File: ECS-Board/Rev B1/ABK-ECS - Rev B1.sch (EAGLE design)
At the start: 298 parts, among them J1 USB-B-S-RA, J10 FTSH-105-01-L-DV-NOPASTE, J11 22-05-7028-02, J12 RB1-125BAG1A, J13 22-05-7068-06, J14 22-05-7048-04, J15 22-05-7048-04, J16 22-05-7048-04, J2 MSTBA2, J3 22-05-7068-06, J5 22-05-7068-06, J6 22-05-7068-06, J7 22-05-7068-06, J8 22-05-7028-02, J9 FTSH-103-01-L-DV-NOPASTE, SW1 B3FS-1015, SW2 B3FS-1015, T1 MMBT2907ALT3, T10 MMBT2222AL, T11 IRLML5103TRPBF, T12 MMBT2222AL, T13 IRLML5103TRPBF, T14 IRLML5103TRPBF, T15 IRLML5103TRPBF, T16 IRLML5103TRPBF, T17 MMBT2222AL, T18 MMBT2222AL, T19 MMBT2222AL, T2 EXMACHINA-LOGO-NAME, T20 MMBT2222AL, T3 IRLML5103TRPBF, T4 IRLML5103TRPBF, T5 IRLML5103TRPBF, T6 IRLML5103TRPBF, T7 MMBT2222AL, T8 MMBT2222AL, T9 MMBT2222AL, U1 AT24C512C-SSHM-B, U10 SN74LVC2G17DBVR, U2 LPC1768FBD100, U3 LT3686HDDPBF, U4 LT3686HDDPBF, U5 CD4050BD, U6 CD4050BD, U7 DP83848JSQ/NOPB, U9 SN74LVC2G17DBVR, X1 FC-135, X2 ASE-12, X3 3000, X4 ASE_50

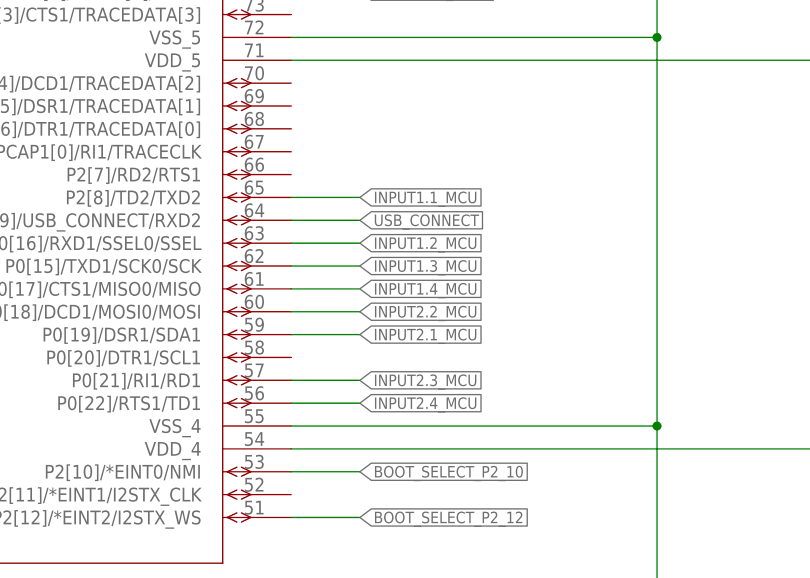
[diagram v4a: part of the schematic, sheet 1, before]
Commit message: Re-Map MCU output signal
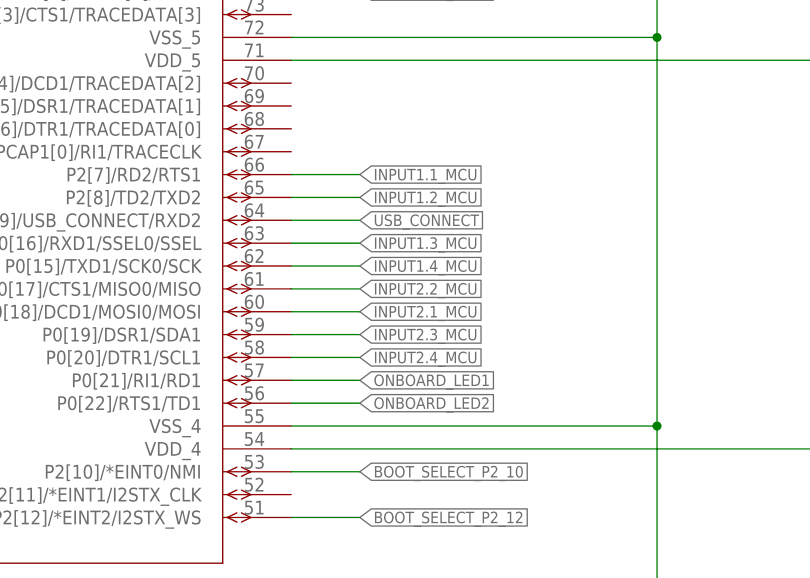
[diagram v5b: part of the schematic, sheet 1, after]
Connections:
- net INPUT1.1_MCU: now also U2.P2[7]/RD2/RTS1; no longer U2.P2[8]/TD2/TXD2
- net INPUT1.2_MCU: now also U2.P2[8]/TD2/TXD2; no longer U2.P0[16]/RXD1/SSEL0/SSEL
- net INPUT1.3_MCU: now also U2.P0[16]/RXD1/SSEL0/SSEL; no longer U2.P0[15]/TXD1/SCK0/SCK
- net INPUT1.4_MCU: now also U2.P0[15]/TXD1/SCK0/SCK; no longer U2.P0[17]/CTS1/MISO0/MISO
- net INPUT2.1_MCU: now also U2.P0[18]/DCD1/MOSI0/MOSI; no longer U2.P0[19]/DSR1/SDA1
- net INPUT2.2_MCU: now also U2.P0[17]/CTS1/MISO0/MISO; no longer U2.P0[18]/DCD1/MOSI0/MOSI
- net INPUT2.3_MCU: now also U2.P0[19]/DSR1/SDA1; no longer U2.P0[21]/RI1/RD1
- net INPUT2.4_MCU: now also U2.P0[20]/DTR1/SCL1; no longer U2.P0[22]/RTS1/TD1
- net ONBOARD_LED1: now also U2.P0[21]/RI1/RD1
- net ONBOARD_LED2: now also U2.P0[22]/RTS1/TD1
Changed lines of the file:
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@@
 <label x="325.12" y="170.18" size="1.27" layer="95" font="vector" xref="yes"/>
+</segment>
+<segment>
+<wire x1="325.12" y1="124.46" x2="317.5" y2="124.46" width="0.1524" layer="91"/>
+<label x="325.12" y="124.46" size="1.27" layer="95" font="vector" xref="yes"/>
+<pinref part="U2" gate="A" pin="P0[21]/RI1/RD1"/>
 </segment>
 </net>
@@
 <label x="325.12" y="167.64" size="1.27" layer="95" font="vector" xref="yes"/>
 </segment>
+<segment>
+<wire x1="325.12" y1="121.92" x2="317.5" y2="121.92" width="0.1524" layer="91"/>
+<label x="325.12" y="121.92" size="1.27" layer="95" font="vector" xref="yes"/>
+<pinref part="U2" gate="A" pin="P0[22]/RTS1/TD1"/>
+</segment>
 </net>
 <net name="!JTAG_TRST" class="0">
@@
 <net name="INPUT2.3_MCU" class="0">
 <segment>
-<pinref part="U2" gate="A" pin="P0[21]/RI1/RD1"/>
-<wire x1="317.5" y1="124.46" x2="325.12" y2="124.46" width="0.1524" layer="91"/>
-<label x="325.12" y="124.46" size="1.27" layer="95" font="vector" xref="yes"/>
-</segment>
-</net>
-<net name="INPUT2.1_MCU" class="0">
-<segment>
-<pinref part="U2" gate="A" pin="P0[19]/DSR1/SDA1"/>
 <wire x1="317.5" y1="129.54" x2="325.12" y2="129.54" width="0.1524" layer="91"/>
 <label x="325.12" y="129.54" size="1.27" layer="95" font="vector" xref="yes"/>
-</segment>
-</net>
-<net name="INPUT2.2_MCU" class="0">
-<segment>
-<pinref part="U2" gate="A" pin="P0[18]/DCD1/MOSI0/MOSI"/>
+<pinref part="U2" gate="A" pin="P0[19]/DSR1/SDA1"/>
+</segment>
+</net>
+<net name="INPUT2.1_MCU" class="0">
+<segment>
 <wire x1="317.5" y1="132.08" x2="325.12" y2="132.08" width="0.1524" layer="91"/>
 <label x="325.12" y="132.08" size="1.27" layer="95" font="vector" xref="yes"/>
+<pinref part="U2" gate="A" pin="P0[18]/DCD1/MOSI0/MOSI"/>
+</segment>
+</net>
+<net name="INPUT2.2_MCU" class="0">
+<segment>
+<wire x1="317.5" y1="134.62" x2="325.12" y2="134.62" width="0.1524" layer="91"/>
+<label x="325.12" y="134.62" size="1.27" layer="95" font="vector" xref="yes"/>
+<pinref part="U2" gate="A" pin="P0[17]/CTS1/MISO0/MISO"/>
 </segment>
 </net>
 <net name="INPUT2.4_MCU" class="0">
 <segment>
-<pinref part="U2" gate="A" pin="P0[22]/RTS1/TD1"/>
-<wire x1="317.5" y1="121.92" x2="325.12" y2="121.92" width="0.1524" layer="91"/>
-<label x="325.12" y="121.92" size="1.27" layer="95" font="vector" xref="yes"/>
+<wire x1="317.5" y1="127" x2="325.12" y2="127" width="0.1524" layer="91"/>
+<label x="325.12" y="127" size="1.27" layer="95" font="vector" xref="yes"/>
+<pinref part="U2" gate="A" pin="P0[20]/DTR1/SCL1"/>
 </segment>
 </net>
@@
 <net name="INPUT1.4_MCU" class="0">
 <segment>
-<wire x1="325.12" y1="134.62" x2="317.5" y2="134.62" width="0.1524" layer="91"/>
-<label x="325.12" y="134.62" size="1.27" layer="95" font="vector" xref="yes"/>
-<pinref part="U2" gate="A" pin="P0[17]/CTS1/MISO0/MISO"/>
+<wire x1="325.12" y1="137.16" x2="317.5" y2="137.16" width="0.1524" layer="91"/>
+<label x="325.12" y="137.16" size="1.27" layer="95" font="vector" xref="yes"/>
+<pinref part="U2" gate="A" pin="P0[15]/TXD1/SCK0/SCK"/>
 </segment>
 </net>
 <net name="INPUT1.2_MCU" class="0">
 <segment>
-<pinref part="U2" gate="A" pin="P0[16]/RXD1/SSEL0/SSEL"/>
+<wire x1="317.5" y1="144.78" x2="325.12" y2="144.78" width="0.1524" layer="91"/>
+<label x="325.12" y="144.78" size="1.27" layer="95" font="vector" xref="yes"/>
+<pinref part="U2" gate="A" pin="P2[8]/TD2/TXD2"/>
+</segment>
+</net>
+<net name="INPUT1.3_MCU" class="0">
+<segment>
 <wire x1="317.5" y1="139.7" x2="325.12" y2="139.7" width="0.1524" layer="91"/>
 <label x="325.12" y="139.7" size="1.27" layer="95" font="vector" xref="yes"/>
-</segment>
-</net>
-<net name="INPUT1.3_MCU" class="0">
-<segment>
-<wire x1="317.5" y1="137.16" x2="325.12" y2="137.16" width="0.1524" layer="91"/>
-<label x="325.12" y="137.16" size="1.27" layer="95" font="vector" xref="yes"/>
-<pinref part="U2" gate="A" pin="P0[15]/TXD1/SCK0/SCK"/>
+<pinref part="U2" gate="A" pin="P0[16]/RXD1/SSEL0/SSEL"/>
 </segment>
 </net>
@@
 <net name="INPUT1.1_MCU" class="0">
 <segment>
-<wire x1="317.5" y1="144.78" x2="325.12" y2="144.78" width="0.1524" layer="91"/>
-<pinref part="U2" gate="A" pin="P2[8]/TD2/TXD2"/>
-<label x="325.12" y="144.78" size="1.27" layer="95" font="vector" xref="yes"/>
-</segment>
-</net>
+<wire x1="317.5" y1="147.32" x2="325.12" y2="147.32" width="0.1524" layer="91"/>
+<label x="325.12" y="147.32" size="1.27" layer="95" font="vector" xref="yes"/>
+<pinref part="U2" gate="A" pin="P2[7]/RD2/RTS1"/>
+</segment>
+</net>

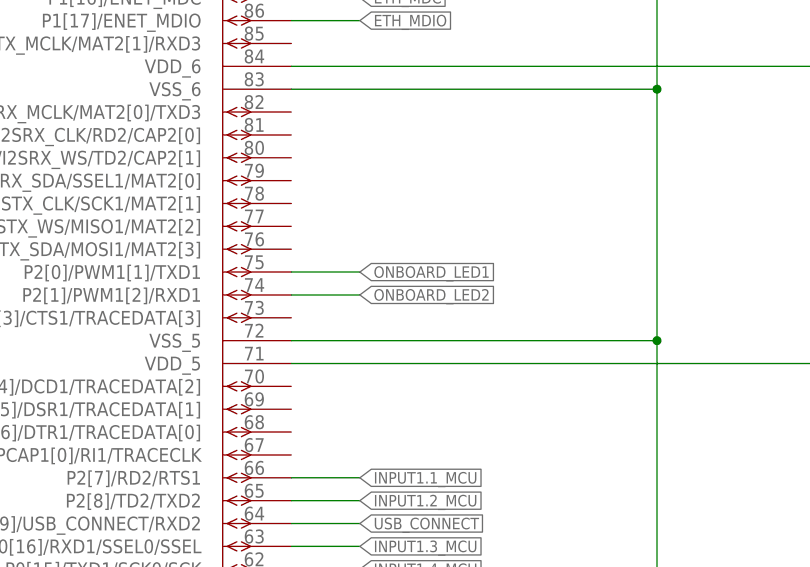
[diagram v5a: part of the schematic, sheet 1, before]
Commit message: Route Reset and all airwire
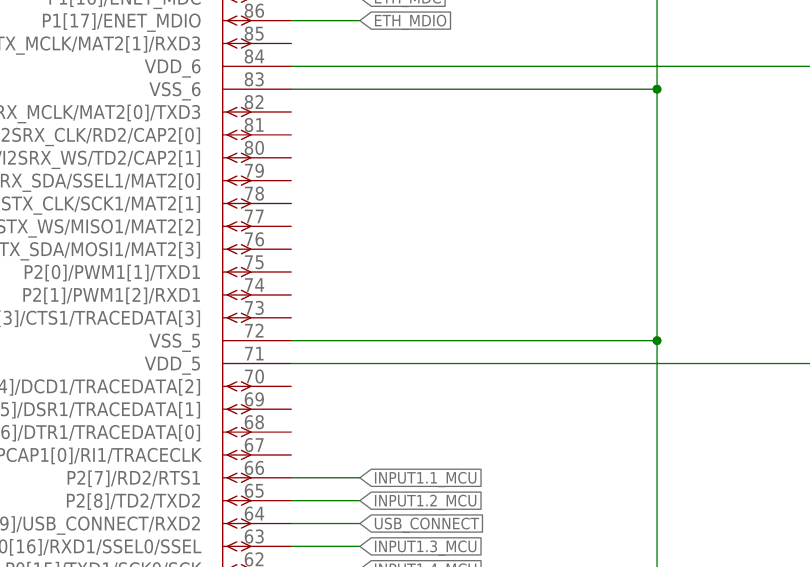
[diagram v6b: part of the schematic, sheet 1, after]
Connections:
- net ONBOARD_LED1: no longer U2.P2[0]/PWM1[1]/TXD1
- net ONBOARD_LED2: no longer U2.P2[1]/PWM1[2]/RXD1
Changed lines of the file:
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@@
-</segment>
-<segment>
-<wire x1="325.12" y1="170.18" x2="317.5" y2="170.18" width="0.1524" layer="91"/>
-<pinref part="U2" gate="A" pin="P2[0]/PWM1[1]/TXD1"/>
-<label x="325.12" y="170.18" size="1.27" layer="95" font="vector" xref="yes"/>
 </segment>
 <segment>
@@
 </segment>
 <segment>
-<wire x1="325.12" y1="167.64" x2="317.5" y2="167.64" width="0.1524" layer="91"/>
-<pinref part="U2" gate="A" pin="P2[1]/PWM1[2]/RXD1"/>
-<label x="325.12" y="167.64" size="1.27" layer="95" font="vector" xref="yes"/>
-</segment>
-<segment>

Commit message: Improte routing and add Silkscreen
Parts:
- removed C36: 0.1uF, rcl:C-EUC0603
- removed D13: 1N4148WS, diode:1N4148WS
- removed J16: 22-05-7048-04, con-molex:22-05-7048-04
- removed R153, R154: 1K, rcl:R-EU_R0603
- removed U10: SN74LVC2G17DBVR, ti:SN74LVC2G17DBVR
- added C20: 0.1uF, rcl:C-EUC0603
- added D4: 1N4148WS, diode:1N4148WS
- added J4: 22-05-7068-06, con-molex:22-05-7068-06
- added R40: 4K7, rcl:R-EU_R0603
- added R41: 1K, rcl:R-EU_R0603
- added U8: SN74LVC2G17DBVR, ti:SN74LVC2G17DBVR
- C22: value 0.1uF -> 4.7uF; device rcl:C-EUC0603 -> rcl:CPOL-EUCT3216; MPN MC0603B104K160CT -> F931A475MAA; OC_NEWARK 06R4923 -> 58R3271
- C23: value 4.7uF -> 100nF; device rcl:CPOL-EUCT3216 -> rcl:C-EUC0603; MPN F931A475MAA -> MC0603B104K250CT; OC_NEWARK 58R3271 -> 06R4925
- C25, C29: value 100nF -> 10uF; device rcl:C-EUC0603 -> rcl:CPOL-EUCT3216; MPN MC0603B104K250CT -> F931A106MAA; OC_NEWARK 06R4925 -> 58R3260
- C26, C30: value 10uF -> 100nF; device rcl:CPOL-EUCT3216 -> rcl:C-EUC0603; MPN F931A106MAA -> MC0603B104K250CT; OC_NEWARK 58R3260 -> 06R4925
- C34: value 100nF -> 0.1uF; MPN MC0603B104K250CT -> MC0603B104K160CT; OC_NEWARK 06R4925 -> 06R4923
- J10: value FTSH-105-01-L-DV-NOPASTE -> 22-05-7028-02; device con-samtec:FTSH-105-01-L-DV-NOPASTE -> con-molex:22-05-7028-02; MPN (none) -> 22-05-7028; OC_NEWARK (none) -> 25M1728
- J11: value 22-05-7028-02 -> RB1-125BAG1A; device con-molex:22-05-7028-02 -> con-wiznet:RB1-125BAG1A; MPN 22-05-7028 -> (none); OC_NEWARK 25M1728 -> unknown
- J12: value RB1-125BAG1A -> 22-05-7068-06; device con-wiznet:RB1-125BAG1A -> con-molex:22-05-7068-06; MF (none) -> MOLEX; MPN (none) -> 22-05-7058; OC_NEWARK unknown -> 55H9619
- J13: value 22-05-7068-06 -> 22-05-7048-04; device con-molex:22-05-7068-06 -> con-molex:22-05-7048-04; MF MOLEX -> (none); MPN 22-05-7058 -> (none); OC_NEWARK 55H9619 -> (none)
- J7: value 22-05-7068-06 -> 22-05-7028-02; device con-molex:22-05-7068-06 -> con-molex:22-05-7028-02; MPN (none) -> 22-05-7028; OC_NEWARK (none) -> 25M1728
- J8: value 22-05-7028-02 -> FTSH-103-01-L-DV-NOPASTE; device con-molex:22-05-7028-02 -> con-samtec:FTSH-103-01-L-DV-NOPASTE; MPN 22-05-7028 -> (none); OC_NEWARK 25M1728 -> (none)
- J9: value FTSH-103-01-L-DV-NOPASTE -> FTSH-105-01-L-DV-NOPASTE; device con-samtec:FTSH-103-01-L-DV-NOPASTE -> con-samtec:FTSH-105-01-L-DV-NOPASTE
- LED3: value Red -> Blue; MPN OVS-0608 -> OVS-0603; OC_NEWARK 15R2208 -> 15R2205
- LED4: value Blue -> Red; MPN OVS-0603 -> OVS-0608; OC_NEWARK 15R2205 -> 15R2208
- LED5: OC_FARNELL 1716771 -> (none)
- LED7: OC_FARNELL (none) -> 1716771
- MP1, MP2, MP3, MP4: value MOUNT-PAD3,0 -> MOUNT-PAD3.5; device holes:MOUNT-PAD3,0 -> holes:MOUNT-PAD3.5
- R10: value 10K -> 33; MPN RC0603FR-0710KL -> RC0603FR-0733RL; OC_NEWARK 68R0049 -> 68R0085
- R101, R70: value 10K -> 1K; MPN RC0603FR-0710KL -> RC0603FR-071KL; OC_NEWARK 68R0049 -> 68R0042
- R105, R74: value 1K -> 1K5; MPN RC0603FR-071KL -> RC0603FR-071K5L; OC_NEWARK 68R0042 -> 68R0045
- R109, R39, R78: value 1K5 -> 4K7; MPN RC0603FR-071K5L -> RC0603FR-074K7L; OC_NEWARK 68R0045 -> 68R0092
- R11: value 0R -> 33; MPN RC0603FR-070RL -> RC0603FR-0733RL; OC_NEWARK 50Y7761 -> 68R0085
- R113, R82: value 4K7 -> 100; MPN RC0603FR-074K7L -> RC0603FR-13100RL; OC_NEWARK 68R0092 -> 68R0131
- R117, R86: value 100 -> 330; MPN RC0603FR-13100RL -> RC0603FR-07330RL; OC_NEWARK 68R0131 -> 98K7391
- R12: value 0R -> 1K5; MPN RC0603FR-070RL -> RC0603FR-071K5L; OC_NEWARK 50Y7761 -> 68R0045
- R121: value 330 -> 0R; MPN RC0603FR-07330RL -> MCMR06X000 PTL; OC_NEWARK 98K7391 -> 86T3500
- R123: value 0R -> 220; MPN MCMR06X000 PTL -> MCMR06X2200FTL; OC_NEWARK 86T3500 -> 86T3577
- R125: value 220 -> 49.9; MPN MCMR06X2200FTL -> MCMR06X49R9FTL; OC_NEWARK 86T3577 -> 86T3659
- R129: value 49.9 -> 4K7; MPN MCMR06X49R9FTL -> MCMR06X4701FTL; OC_NEWARK 86T3659 -> 86T3649
- R130: value 4K7 -> 2K2; MPN MCMR06X4701FTL -> MCMR06X2201FTL; OC_NEWARK 86T3649 -> 86T3578
- R131: value 2K2 -> 1K; MPN MCMR06X2201FTL -> MCMR06X1001FTL; OC_NEWARK 86T3578 -> 86T3505
- R132: value 0R, DNI -> 1K; MPN RC0603FR-070RL -> MCMR06X1001FTL; OC_NEWARK 50Y7761 -> 86T3505
- R133, R138: value 4K7 -> 1K; MPN MCMR06X2701FTL -> MCMR06X1001FTL; OC_NEWARK 86T3598 -> 86T3505
- R134, R144: value 1K -> 4K7; MPN MCMR06X1001FTL -> MCMR06X2701FTL; OC_NEWARK 86T3505 -> 86T3598
- R14, R15: value 1K5 -> 0R; MPN RC0603FR-071K5L -> RC0603FR-070RL; OC_NEWARK 68R0045 -> 50Y7761
- R16: value 31K6 -> 10K; MPN MCMR06X3162FTL -> RC0603FR-0710KL; OC_FARNELL 2073391 -> (none); OC_NEWARK 86T3613 -> 68R0049
- R17: value 31K6 -> 1K5; MPN MCMR06X3162FTL -> RC0603FR-071K5L; OC_FARNELL 2073391 -> (none); OC_NEWARK 86T3613 -> 68R0045
- R18, R53: value 4K7 -> 1K5; MPN RC0603FR-074K7L -> RC0603FR-071K5L; OC_NEWARK 68R0092 -> 68R0045
- R19: value 4K7 -> 31K6; MPN RC0603FR-074K7L -> MCMR06X3162FTL; OC_FARNELL (none) -> 2073391; OC_NEWARK 68R0092 -> 86T3613
- R20: value 52K3 -> 31K6; MPN MC0063W0603152K3 -> MCMR06X3162FTL; OC_NEWARK 26M0962 -> 86T3613
- R21: value 10K -> 4K7; MPN RC0603FR-0710KL -> RC0603FR-074K7L; OC_FARNELL 2073391 -> (none); OC_NEWARK 68R0049 -> 68R0092
- R22: value 31K6 -> 4K7; MPN MCMR06X3162FTL -> RC0603FR-074K7L; OC_FARNELL 2073391 -> (none); OC_NEWARK 86T3613 -> 68R0092
- R23: value 10K -> 52K3; MPN RC0603FR-0710KL -> MC0063W0603152K3; OC_NEWARK 68R0049 -> 26M0962
- R24: value 1K5 -> 10K; MPN RC0603FR-071K5L -> RC0603FR-0710KL; OC_NEWARK 68R0045 -> 68R0049
- R25: value 1K5 -> 31K6; MPN RC0603FR-071K5L -> MCMR06X3162FTL; OC_NEWARK 68R0045 -> 86T3613
- R26: value 1K5 -> 10K; MPN RC0603FR-071K5L -> RC0603FR-0710KL; OC_FARNELL (none) -> 2073391; OC_NEWARK 68R0045 -> 68R0049
- R27, R28: value 1K -> 1K5; MPN RC0603FR-071KL -> RC0603FR-071K5L; OC_FARNELL (none) -> 2073391; OC_NEWARK 68R0042 -> 68R0045
- R35, R36: value 4K7 -> 1K; MPN RC0603FR-074K7L -> RC0603FR-071KL; OC_NEWARK 68R0092 -> 68R0042
- R49: value 1K -> 4K7; MPN RC0603FR-071KL -> RC0603FR-074K7L; OC_NEWARK 68R0042 -> 68R0092
- R5: value 39K -> 1K5; MPN (none) -> RC0603FR-071K5L; OC_NEWARK (none) -> 68R0045
- R6: value 24K -> 1K5; MPN (none) -> RC0603FR-071K5L; OC_NEWARK (none) -> 68R0045
- R62: value 1K5 -> 1K; device rcl:R-EU_R0603 -> rcl:R-EU_R1206; MPN RC0603FR-071K5L -> (none); OC_NEWARK 68R0045 -> (none)
- R66, R91, R97: value 1K -> 10K; device rcl:R-EU_R1206 -> rcl:R-EU_R0603; MPN (none) -> RC0603FR-0710KL; OC_NEWARK (none) -> 68R0049
- R7: value 33 -> 39K; MPN RC0603FR-0733RL -> (none); OC_NEWARK 68R0085 -> (none)
- R8: value 33 -> 24K; MPN RC0603FR-0733RL -> (none); OC_NEWARK 68R0085 -> (none)
- R9: value 1K5 -> 0R, DNI; MPN RC0603FR-071K5L -> RC0603FR-070RL; OC_NEWARK 68R0045 -> 50Y7761
- R90: value 330 -> 1K; device rcl:R-EU_R0603 -> rcl:R-EU_R1206; MPN RC0603FR-07330RL -> (none); OC_NEWARK 98K7391 -> (none)
- R92: value 10K -> 100; MPN RC0603FR-0710KL -> RC0603FR-13100RL; OC_NEWARK 68R0049 -> 68R0131
- R93: value 100 -> 1K; device rcl:R-EU_R0603 -> rcl:R-EU_R1206; MPN RC0603FR-13100RL -> (none); OC_NEWARK 68R0131 -> (none)
- SJ1, SJ2: value SOLDERJUMPERNC -> SJNC; device SparkFun-Passives:SOLDERJUMPERNC -> SparkFun-Passives:SJNC; OC_NEWARK unknown -> (none)
- SJ3, SJ4, SJ5: value SOLDERJUMPERNC -> SJNC; device SparkFun-Passives:SOLDERJUMPERNC -> SparkFun-Passives:SJNC
- SJ6, SJ7: OC_NEWARK (none) -> unknown
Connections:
- removed net N$3 (its old number): LED2.C, R15.1
- new net N$45: LED4.C, R21.1
- net !ISP_BOOT: now also J8-2.S, R121.2; no longer J9-2.S, R122.2
- net !ISP_RST: now also J8-6.S, R122.2; no longer J9-6.S, R123.2
- net !RESET: now also J9-10.S, R122.1, R16.1; no longer J10-10.S, R123.1, R13.1
- net +24V: now also J4-1.S, R21.2, R22.2, R66.2, R91.2, R97.2; no longer J7-1.S, R101.2, R18.2, R19.2, R70.2, R92.2
- net +3V3: now also C20.1, C22.+, C23.1, C29.+, C30.1, J11.CT, J14-1.S, J8-1.S, R123.2, R125.1, R130.1, R140.1, R142.1, R145.1, R147.1, R16.2, R28.2, R5.1, R9.1, U8.VCC; no longer C22.1, C23.+, C25.1, C30.+, C36.1, J10-1.S, J12.CT, J16-1.S, R10.2, R125.2, R129.1, R131.1, R132.1, R149.1, R150.1, R153.1, R154.1, R22.2, R26.1, U10.VCC
- net +5V: now also J10-1.S, J12-1.S, R134.1, R144.1, R23.2, R27.2; no longer J11-1.S, J13-6.S, R133.1, R138.1, R20.2, R24.2
- net 1: now also SJ4.2; no longer SJ2.2
- net 2: now also SJ5.2; no longer SJ3.2
- net 3: now also SJ6.2; no longer SJ4.2
- net 4: now also SJ7.2; no longer SJ5.2
- net ADC1: now also R136.2; no longer R142.2
- net ADC2: now also R133.2; no longer R141.2
- net AGND: now also J11.P$1; no longer J12.P$1
- net BOOT_SELECT_P2_10: now also R121.1, R14.1; no longer R11.1, R122.1
- net BOOT_SELECT_P2_12: now also R15.1; no longer R12.1
- net ENCODER_A: now also U8.1Y; no longer U9.1Y
- net ENCODER_B: now also U8.2Y; no longer U9.2Y
- net ENCODER_PUSH: now also U9.2Y; no longer U10.2Y
- net ENCODER_Z: now also U9.1Y; no longer U10.1Y
- net ETH_RX_N: now also J11.RD-, R128.2; no longer J12.RD-, R129.2
- net ETH_RX_P: now also J11.RD+, R127.2; no longer J12.RD+, R128.2
- net ETH_TX_N: now also J11.TD-, R126.2; no longer J12.TD-, R127.2
- net ETH_TX_P: now also J11.TD+, R125.2; no longer J12.TD+, R126.2
- net GND: now also C20.2, C22.-, C23.2, C25.-, C26.2, C29.-, C30.2, D4.2, J10-2.S, J11.R4, J11.R5, J11.R6, J12-6.S, J13-4.S, J4-6.S, J7-2.S, J8-5.S, J9-3.S, J9-7.S, J9-9.S, LED7.C, R105.2, R129.2, R141.1, R143.1, R146.1, R17.2, R18.2, R19.1, R20.1, R24.1, R26.1, R40.2, R49.2, R6.2, R62.1, R7.1, R74.2, R90.1, R93.1, SJ6.1, SJ7.1, U8.GND; no longer C22.2, C23.-, C25.2, C26.-, C29.2, C30.-, C36.2, D13.2, J10-3.S, J10-5.S, J10-7.S, J10-9.S, J11-2.S, J12.R4, J12.R5, J12.R6, J13-1.S, J16-4.S, J7-6.S, J8-2.S, LED4.C, R113.2, R130.2, R14.2, R147.1, R15.2, R151.1, R152.1, R16.1, R17.1, R21.1, R23.1, R35.2, R36.2, R5.1, R62.2, R66.1, R82.2, R91.1, R97.1, SJ1.1, SJ2.1, U10.GND
- net I2C_SCL: now also R131.2, R140.2, R141.2; no longer R143.2, R147.2, R149.2
- net I2C_SDA: now also R137.2, R145.2, R146.2; no longer R144.2, R148.2, R150.2
- net INPUT1.1: now also R48.2, R52.1; no longer R49.2, R53.1
- net INPUT1.2: now also R47.2, R51.1; no longer R48.2, R52.1
- net INPUT1.3: now also R46.2, R50.1; no longer R47.2, R51.1
- net INPUT1.4: now also R45.2, R49.1; no longer R46.2, R50.1
- net INPUT2.1: now also R36.2, R40.1; no longer R34.2, R38.1
- net INPUT2.2: now also R35.2, R39.1; no longer R33.2, R37.1
- net INPUT2.3: now also R34.2, R38.1; no longer R32.2, R36.1
- net INPUT2.4: now also R33.2, R37.1; no longer R31.2, R35.1
- net ISP_RXDO: now also J8-4.S; no longer J9-4.S
- net ISP_TXDO: now also J8-3.S; no longer J9-3.S
- net JTAG_TCK: now also J9-4.S; no longer J10-4.S
- net JTAG_TDI: now also J9-8.S; no longer J10-8.S
- net JTAG_TDO: now also J9-6.S; no longer J10-6.S
- net JTAG_TMS: now also J9-2.S; no longer J10-2.S
- net L1_1: now also J11.L2; no longer J12.L2
- net L1_2: now also J11.L4; no longer J12.L4
- net MII_MODE: now also R130.2; no longer R131.2
- net MOTOR_VFQ: now also D8.1, J7-1.S, R90.2; no longer D9.1, J8-1.S, R91.2
- net N$1: now also R11.1, R12.2; no longer R8.1, R9.2
- net N$100: now also R45.1; no longer R46.1
- net N$101: now also R42.2; no longer R43.2
- net N$102: now also J4-4.S, R42.1; no longer J5-4.S, R43.1
- net N$103: now also R46.1; no longer R47.1
- net N$104: now also R43.2; no longer R44.2
- net N$105: now also J4-3.S, R43.1; no longer J5-3.S, R44.1
- net N$106: now also R47.1; no longer R48.1
- net N$107: now also R58.1; no longer R59.1
- net N$108: now also R59.1; no longer R60.1
- net N$109: now also R60.1; no longer R61.1
- net N$110: now also R48.1; no longer R49.1
- net N$111: now also R44.2; no longer R45.2
- net N$112: now also J4-2.S, R44.1; no longer J5-2.S, R45.1
- net N$113: now also J11.L1, R123.1; no longer J12.L1, R124.1
- net N$114: now also R8.2; no longer R6.2
- net N$115: now also J11.L3, R124.1; no longer J12.L3, R125.1
- net N$116: now also R129.1; no longer R130.1
- net N$117: now also J12-5.S, R134.2, R151.1; no longer J13-5.S, R133.2, R134.1
- net N$118: now also J12-4.S, R135.2, R149.1; no longer J13-4.S, R136.1, R138.2
- net N$119: now also J12-3.S, R139.2, R152.1; no longer J13-3.S, R135.2, R137.1
- net N$120: now also R150.2, U9.2A; no longer R140.2, U10.2A
- net N$121: now also R149.2, U8.2A; no longer R136.2, U9.2A
- net N$122: now also R151.2, U8.1A; no longer R134.2, U9.1A
- net N$123: now also R152.2, U9.1A; no longer R137.2, U10.1A
- net N$124: now also J12-2.S, R144.2, R150.1; no longer J13-2.S, R139.2, R140.1
- net N$125: now also J13-2.S, R133.1; no longer J14-2.S, R141.1
- net N$126: now also J13-3.S, R136.1; no longer J14-3.S, R142.1
- net N$127: now also J14-2.S, R131.1; no longer J15-2.S, R143.1
- net N$128: now also J14-3.S, R137.1; no longer J15-3.S, R144.1
- net N$129: now also J15-2.S, R132.1; no longer J16-2.S, R145.1
- net N$13: now also R25.1, R26.2; no longer R22.1, R23.2
- net N$130: now also J15-3.S, R138.1; no longer J16-3.S, R146.1
- net N$17: now also R101.2; no longer R102.2
- net N$18: now also R97.1; no longer R98.1
- net N$19: now also R102.2; no longer R103.2
- net N$2: now also R10.1; no longer R7.1
- net N$20: now also R98.1; no longer R99.1
- net N$21: now also R103.2; no longer R104.2
- net N$22: now also R99.1; no longer R100.1
- net N$23: now also R104.2; no longer R105.2
- net N$24: now also R100.1; no longer R101.1
- net N$25: now also R92.1; no longer R93.1
- net N$26: now also R91.1; no longer R92.1
- net N$28: now also LED1.A, R5.2, SJ1.2; no longer LED7.A, R26.2, SJ6.2
- net N$29: now also LED2.C, R17.1; no longer LED1.C, R14.1
- net N$30: now also R12.1, R9.2; no longer R132.2, R9.1
- net N$31: now also R70.1, R78.1, R82.1; no longer R71.1, R79.1, R83.1
- net N$32: now also LED1.C, R6.1, SJ2.2; no longer LED7.C, R39.1, SJ7.2
- net N$33: now also R82.2; no longer R83.2
- net N$34: now also R71.1, R79.1, R83.1; no longer R72.1, R80.1, R84.1
- net N$35: now also R83.2; no longer R84.2
- net N$36: now also R72.1, R80.1, R84.1; no longer R73.1, R81.1, R85.1
- net N$37: now also R73.1, R81.1, R85.1; no longer R74.1, R82.1, R86.1
- net N$38: now also R84.2; no longer R85.2
- net N$39: now also R85.2; no longer R86.2
- net N$4: now also R19.2; no longer R16.2
- net N$40: now also R86.1; no longer R87.1
- net N$41: now also R29.2; no longer R27.2
- net N$42: now also R87.1; no longer R88.1
- net N$43: now also R89.1; no longer R90.1
- net N$44: now also LED5.A, R22.1; no longer LED4.A, R19.1
- net N$46: now also R88.1; no longer R89.1
- net N$47: now also R30.2; no longer R28.2
- net N$48: now also R31.2; no longer R29.2
- net N$49: now also R32.2; no longer R30.2
- net N$5: now also R13.1, R14.2, R15.2; no longer R10.1, R11.2, R12.2
- net N$50: now also LED7.A, R28.1; no longer LED6.A, R25.1
- net N$51: now also LED6.A, R27.1; no longer LED5.A, R24.1
- net N$52: now also R32.1; no longer R30.1
- net N$53: now also R31.1; no longer R29.1
- net N$54: now also R30.1; no longer R28.1
- net N$55: now also R29.1; no longer R27.1
- net N$56: now also R53.1; no longer R54.1
- net N$57: now also R54.1; no longer R55.1
- net N$58: now also R55.1; no longer R56.1
- net N$59: now also R56.1; no longer R57.1
- net N$61: now also R36.1; no longer R34.1
- net N$62: now also R35.1; no longer R33.1
- net N$63: now also R34.1; no longer R32.1
- net N$64: now also R33.1; no longer R31.1
- net N$65: now also R57.1; no longer R58.1
- net N$66: now also R74.1; no longer R75.1
- net N$67: now also R75.1; no longer R76.1
- net N$68: now also R76.1; no longer R77.1
- net N$69: now also R77.1; no longer R78.1
- net N$7: now also R20.2; no longer R17.2
- net N$70: now also SJ3.2; no longer SJ1.2
- net N$71: now also R66.1; no longer R67.1
- net N$72: now also R67.1; no longer R68.1
- net N$75: now also R101.1, R109.1, R113.1; no longer R102.1, R110.1, R114.1
- net N$76: now also R113.2; no longer R114.2
- net N$77: now also R68.1; no longer R69.1
- net N$78: now also R69.1; no longer R70.1
- net N$79: now also R102.1, R110.1, R114.1; no longer R103.1, R111.1, R115.1
- net N$80: now also R114.2; no longer R115.2
- net N$81: now also R41.2; no longer R42.2
- net N$82: now also J4-5.S, R41.1; no longer J5-5.S, R42.1
- net N$83: now also R103.1, R111.1, R115.1; no longer R104.1, R112.1, R116.1
- net N$84: now also R70.2; no longer R71.2
- net N$85: now also R71.2; no longer R72.2
- net N$86: now also R104.1, R112.1, R116.1; no longer R105.1, R113.1, R117.1
- net N$87: now also R115.2; no longer R116.2
- net N$88: now also R116.2; no longer R117.2
- net N$89: now also R117.1; no longer R118.1
- net N$9: now also R23.1, R24.2; no longer R20.1, R21.2
- net N$90: now also R61.1; no longer R62.1
- net N$91: now also R118.1; no longer R119.1
- net N$92: now also R120.1; no longer R121.1
- net N$93: now also R119.1; no longer R120.1
- net N$94: now also R105.1; no longer R106.1
- net N$95: now also R106.1; no longer R107.1
- net N$96: now also R107.1; no longer R108.1
- net N$97: now also R108.1; no longer R109.1
- net N$98: now also R72.2; no longer R73.2
- net N$99: now also R73.2; no longer R74.2
- net ONBOARD_LED1: now also LED3.A; no longer LED2.A
- net ONBOARD_LED2: now also LED2.A; no longer LED1.A
- net OUTPUT1.1: now also D4.1, J5-2.S, R62.2; no longer D5.1, J6-2.S, R63.2
- net OUTPUT1.1_MCU: now also R86.2; no longer R87.2
- net OUTPUT1.2: now also D5.1, J5-3.S, R63.2; no longer D6.1, J6-3.S, R64.2
- net OUTPUT1.2_MCU: now also R87.2; no longer R88.2
- net OUTPUT1.3: now also D6.1, J5-4.S, R64.2; no longer D7.1, J6-4.S, R65.2
- net OUTPUT1.3_MCU: now also R88.2; no longer R89.2
- net OUTPUT1.4: now also D7.1, J5-5.S, R65.2; no longer D8.1, J6-5.S, R66.2
- net OUTPUT1.4_MCU: now also R89.2; no longer R90.2
- net OUTPUT2.1: now also D9.1, J6-2.S, R93.2; no longer D10.1, J7-2.S, R94.2
- net OUTPUT2.1_MCU: now also R117.2; no longer R118.2
- net OUTPUT2.2: now also D10.1, J6-3.S, R94.2; no longer D11.1, J7-3.S, R95.2
- net OUTPUT2.2_MCU: now also R118.2; no longer R119.2
- net OUTPUT2.3: now also D11.1, J6-4.S, R95.2; no longer D12.1, J7-4.S, R96.2
- net OUTPUT2.3_MCU: now also R119.2; no longer R120.2
- net OUTPUT2.4: now also D12.1, J6-5.S, R96.2; no longer D13.1, J7-5.S, R97.2
- net OUTPUT2.4_MCU: now also R120.2; no longer R121.2
- net OUTPUT3.2_MCU: now also R92.2; no longer R93.2
- net PFBOUT: now also C25.+, C26.1; no longer C26.+, C29.1
- net UART_RX: now also R132.2, R142.2, R143.2; no longer R145.2, R151.2, R153.2
- net UART_TX: now also R138.2, R147.2, R148.2; no longer R146.2, R152.2, R154.2
- net USB_D_N: now also R10.2; no longer R7.2
- net USB_D_P: now also R11.2; no longer R8.2
- net USB_LED: now also SJ1.1, SJ2.1; no longer SJ6.1, SJ7.1
- net USB_V_BUS: now also R7.2, R8.1; no longer R5.2, R6.1
- net VIN: now also LED4.A; no longer LED3.A
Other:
- note added: "If pull-down config : Solder jump SJ1 and R6 mount If pull-up config : Solder jump SJ2 and R5 mount"
